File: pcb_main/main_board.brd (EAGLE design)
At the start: 160 x 100 mm, 14 parts, among them U1 STM32F411RET6

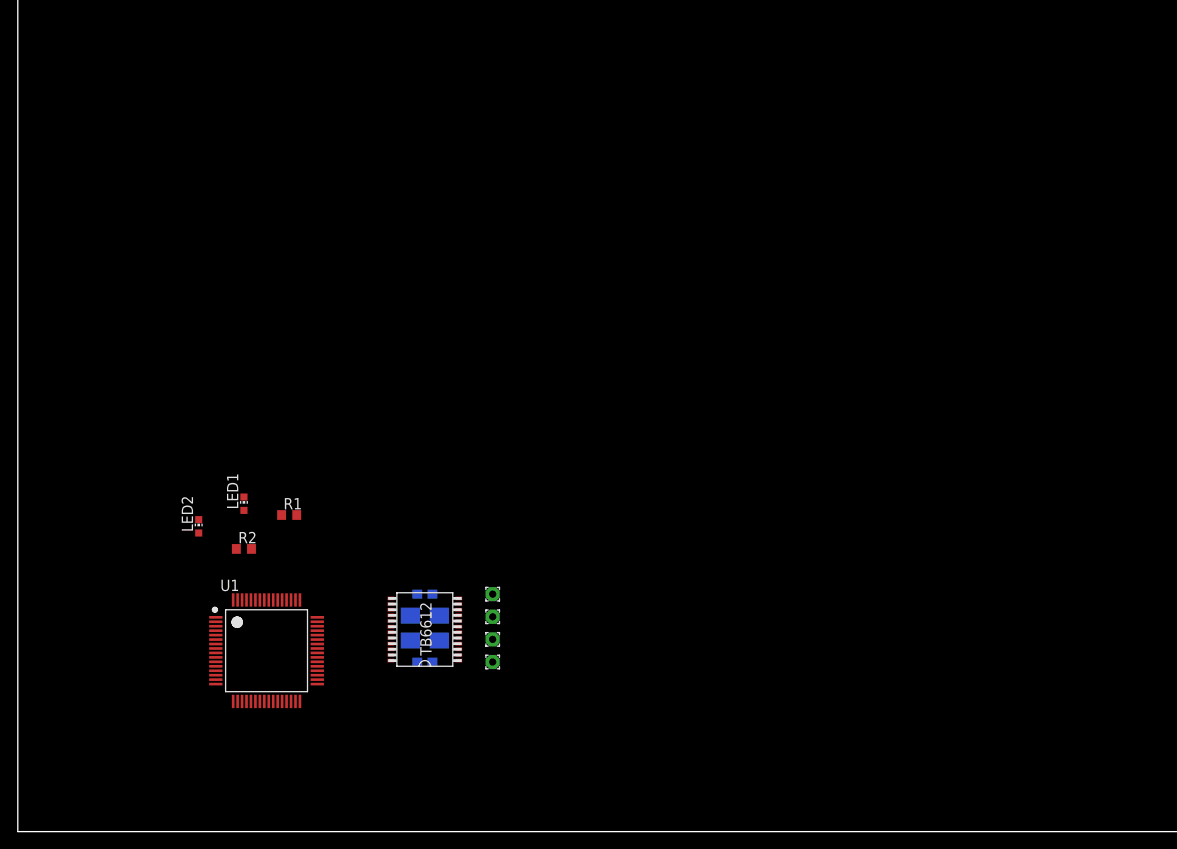
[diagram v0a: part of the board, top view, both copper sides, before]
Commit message: sensors on main pcb
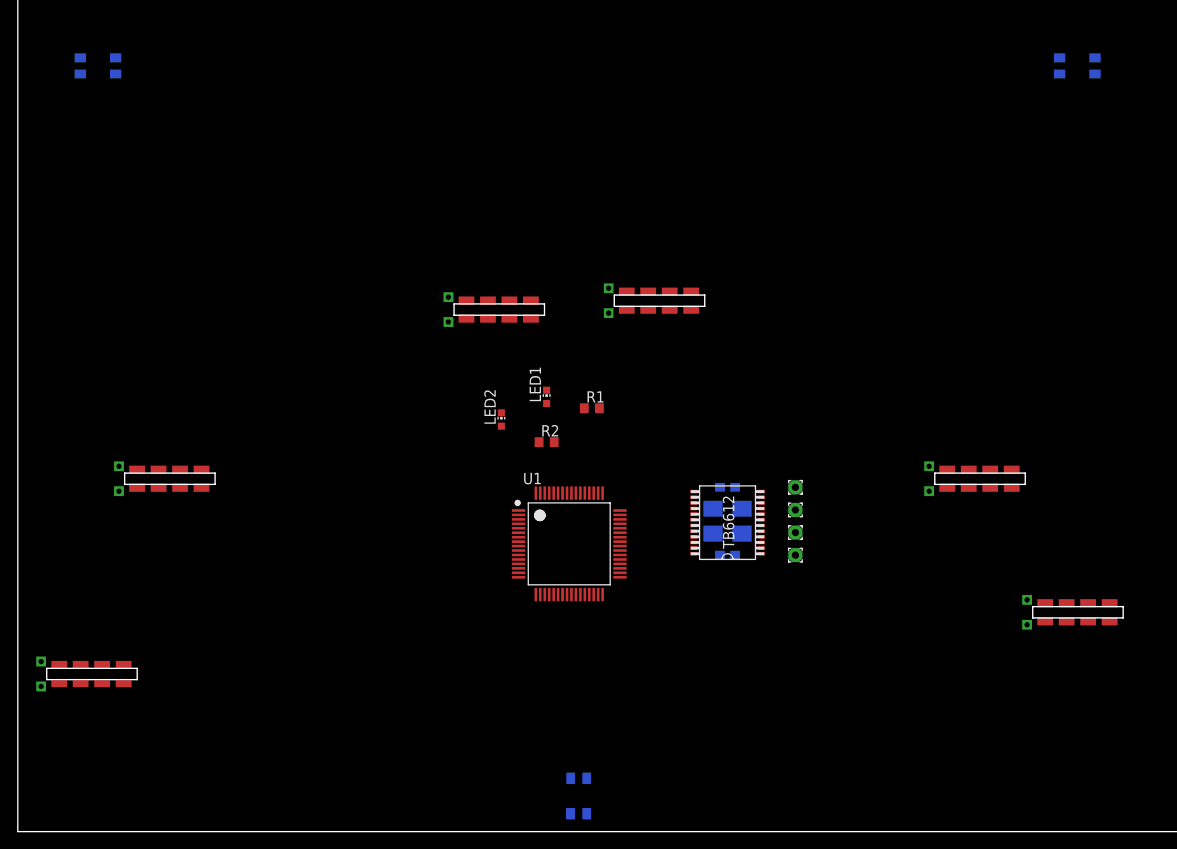
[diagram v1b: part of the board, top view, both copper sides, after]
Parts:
- added CZ1, CZ2, CZ3: KTIR0711S, KTIR0711S:TOP
- added U$1, U$2, U$3, U$4, U$5, U$6: TOF_VL53L0X, TOF_VL53L0X:TOF_VL53L0X
- moved C10 36.1 mm to (79.7, 33.5)
- moved C7 36.1 mm to (79.7, 38.7)
- moved C9 36.1 mm to (79.7, 31.1)
- moved H1 36.1 mm to (87.3, 31.1)
- moved H2 36.1 mm to (87.3, 33.6)
- moved H3 36.1 mm to (87.3, 38.7)
- moved H4 36.1 mm to (87.3, 36.1)
- moved LED1 36.1 mm to (59.4, 48.8)
- moved LED2 36.1 mm to (54.3, 46.3)
- moved R1 36.1 mm to (64.5, 47.6)
- moved R2 36.1 mm to (59.4, 43.8)
- moved TB6612 36.1 mm to (79.7, 34.9)
- moved U1 36.1 mm to (61.9, 32.3)
- moved C8 36.1 mm to (79.7, 36.3)
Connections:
- new net G1: U$1.G
- new net G2: U$2.G
- new net G3: U$3.G
- new net G4: U$6.G
- new net G5: U$5.G
- new net G6: U$4.G
- new net N$3: CZ1.ANODA, CZ2.KATODA
- new net N$4: CZ2.ANODA, CZ3.KATODA
- new net SCL: U$1.SCL, U$1.SCL_, U$2.SCL, U$2.SCL_, U$3.SCL, U$3.SCL_, U$4.SCL, U$4.SCL_, U$5.SCL, U$5.SCL_, U$6.SCL, U$6.SCL_
- new net SDA: U$1.SDA, U$1.SDA_, U$2.SDA, U$2.SDA_, U$3.SDA, U$3.SDA_, U$4.SDA, U$4.SDA_, U$5.SDA, U$5.SDA_, U$6.SDA, U$6.SDA_
- new net X1: U$1.X
- new net X2: U$2.X
- new net X3: U$3.X
- new net X4: U$6.X
- new net X5: U$5.X
- new net X6: U$4.X
- net 3,3V: now also U$1.VCC, U$1.VCC_, U$2.VCC, U$2.VCC_, U$3.VCC, U$3.VCC_, U$4.VCC, U$4.VCC_, U$5.VCC, U$5.VCC_, U$6.VCC, U$6.VCC_
- net GND: now also CZ1.EMITER, CZ2.EMITER, CZ3.EMITER, U$1.GND, U$1.GND_, U$2.GND, U$2.GND_, U$3.GND, U$3.GND_, U$4.GND, U$4.GND_, U$5.GND, U$5.GND_, U$6.GND, U$6.GND_

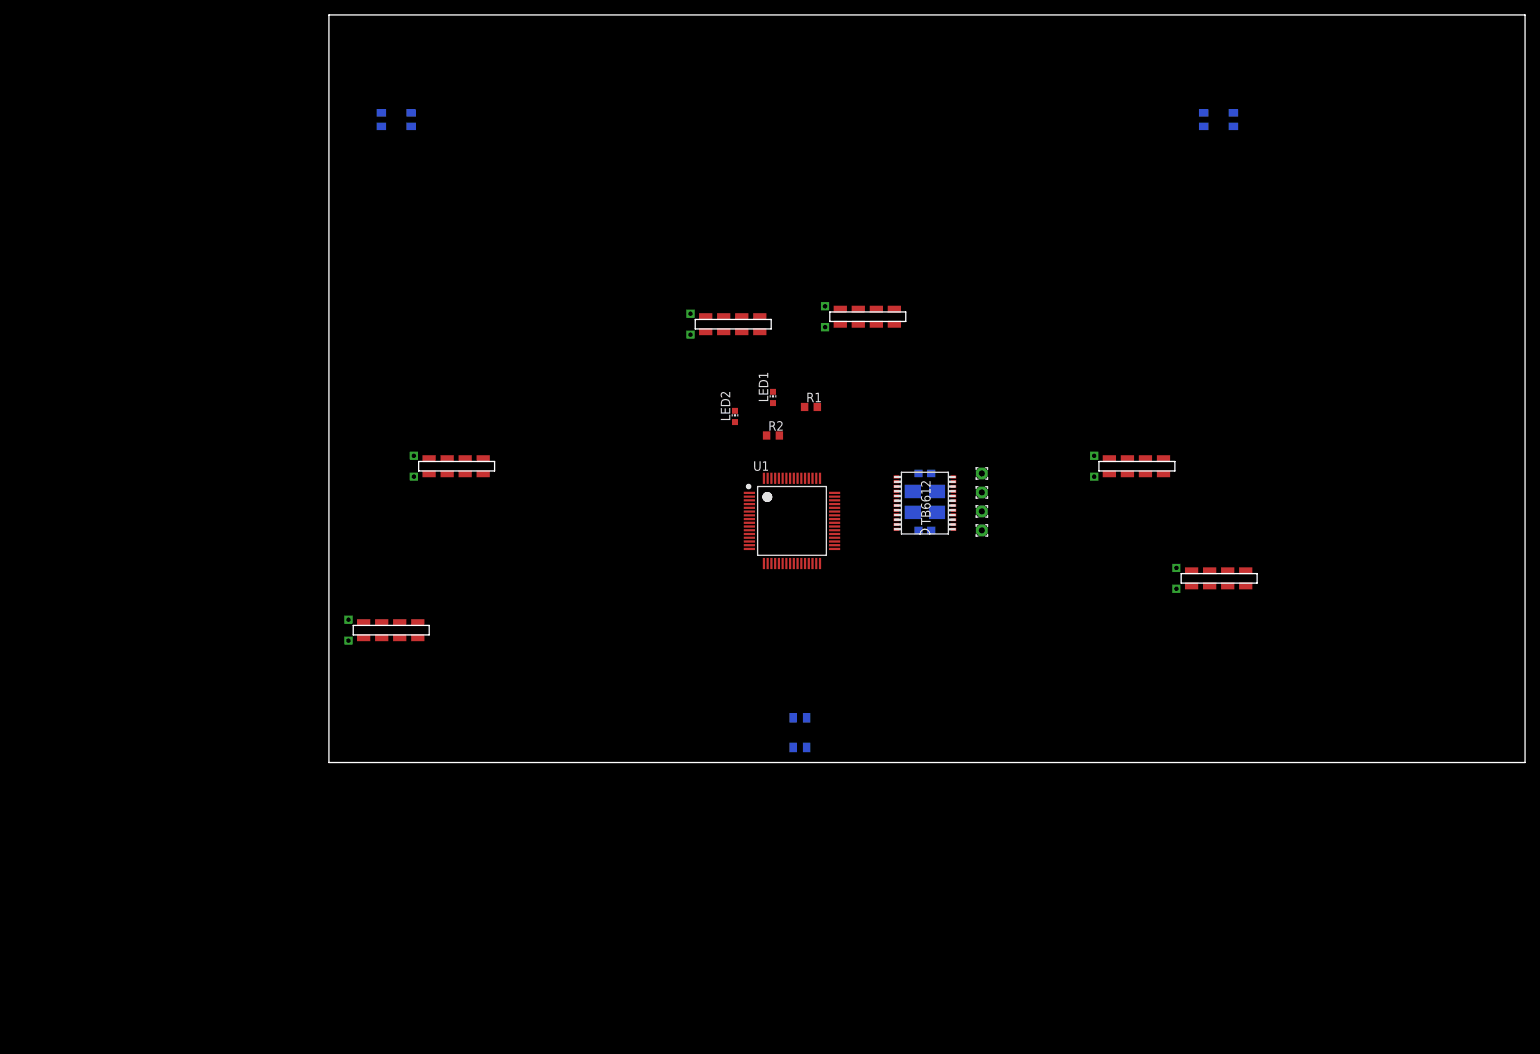
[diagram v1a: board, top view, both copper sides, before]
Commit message: pcb shape
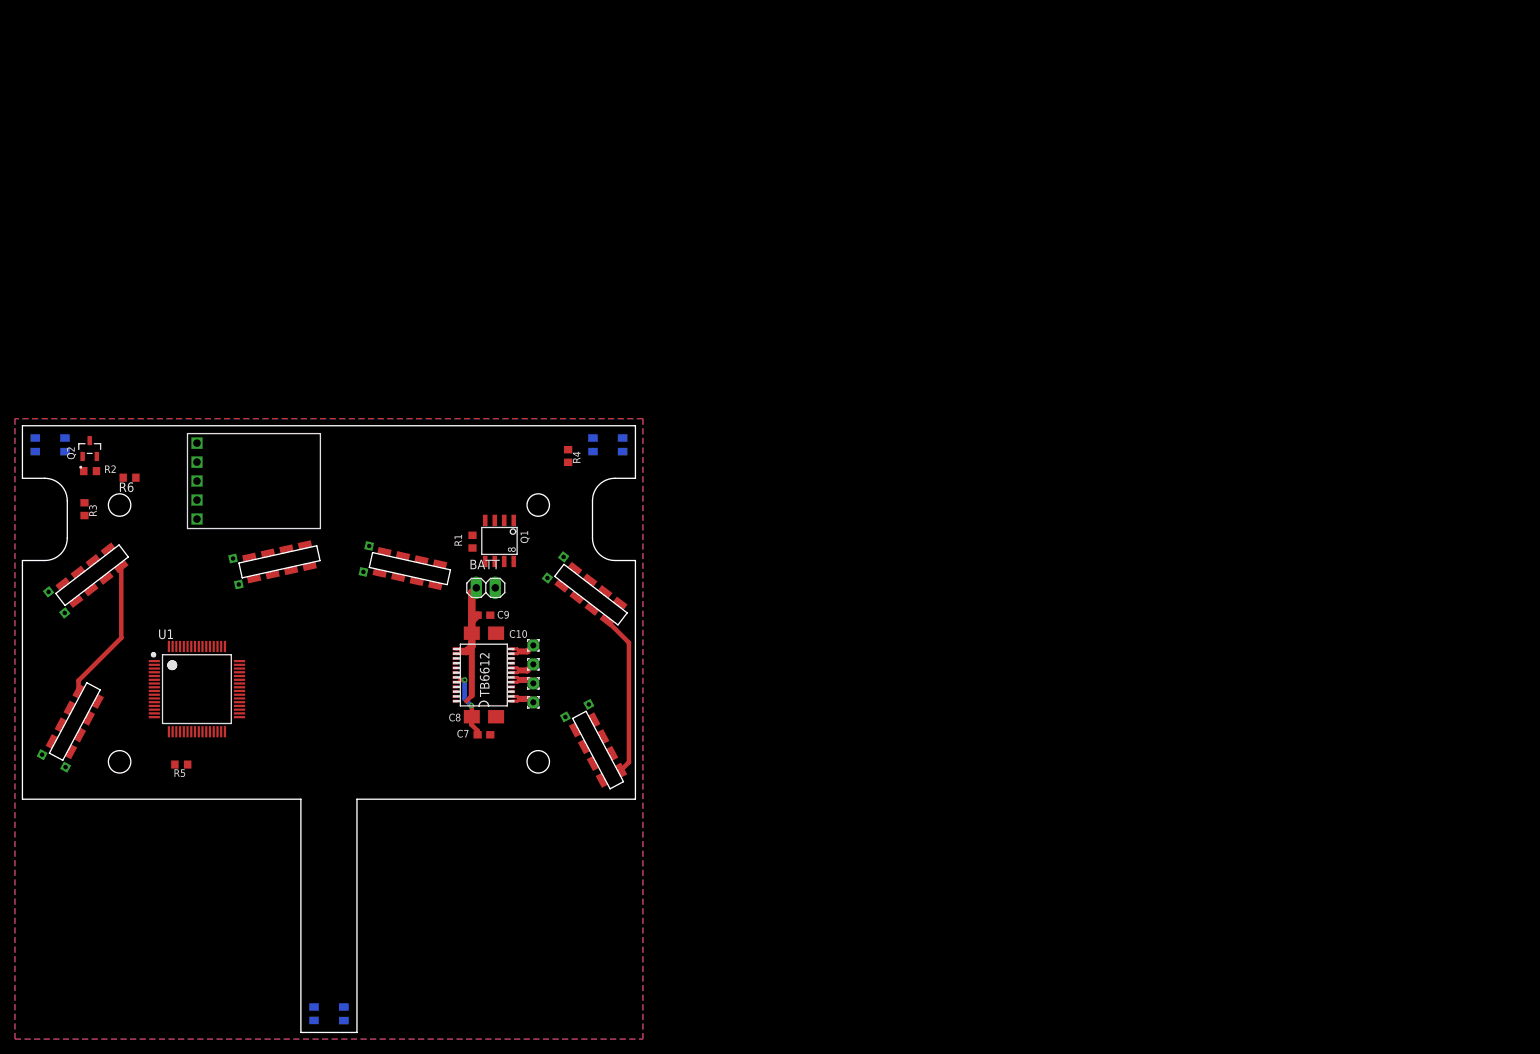
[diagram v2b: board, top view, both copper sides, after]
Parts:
- removed LED1, LED2: (no value), led:CHIP-LED0603
- added BATT: (no value), pinhead:1X02
- added Q1: FDS5680, transistor-fet:SO-8
- added Q2: 2N7002, 2N7002:SOT95P240X111-3N
- added R3, R4, R5: (no value), rcl:R0603
- added R6: 470R, rcl:R0603
- added U$7: D24V10F3-H, D24V10F3:D24V10F3-H
- R2: value (none) -> 10k
- moved CZ2 92.6 mm to (37.3, 42.5), turned to 180 degrees
- moved R2 91.5 mm to (-31.9, 39.0), turned to 180 degrees
- moved U$4 83.4 mm to (32.6, 5.90), turned to 298 degrees
- moved U1 82.7 mm to (-17.7, 9.82)
- moved U$5 74.2 mm to (30.2, 24.9), turned to 322.5 degrees
- moved CZ3 73.4 mm to (0.00, -33.6), turned to 180 degrees
- moved U$6 69.8 mm to (5.40, 26.1), turned to 347.5 degrees
- moved U$3 69.1 mm to (-11.6, 24.7), turned to 12.5 degrees
- moved C7 68.6 mm to (20.7, 3.71), flipped to the top, turned to 0 degrees
- moved C8 66.2 mm to (20.7, 6.12), flipped to the top, turned to 180 degrees
- moved H1 64.3 mm to (27.3, 8.05)
- moved H2 64.3 mm to (27.3, 10.6)
- moved H3 64.3 mm to (27.3, 15.7)
- moved H4 64.3 mm to (27.3, 13.1)
- moved CZ1 63.5 mm to (-37.3, 42.5), turned to 180 degrees
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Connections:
- net !A_DIR renamed A_DIR_1
- net A_DIR renamed A_DIR_2
- removed net +5V: C7.1, C8.+, TB6612.19, TB6612.20
- removed net +BAT: C10.+, C9.1, TB6612.13, TB6612.14, TB6612.24
- new net BAT+: BATT.2, C10.+, C9.1, R1.2, TB6612.13, TB6612.14, TB6612.24, U$7.VIN
- new net BAT-: BATT.1, Q1.5, Q1.6, Q1.7, Q1.8
- new net LS1: CZ1.KOLEKTOR, R3.1
- new net LS2: CZ2.KOLEKTOR, R4.1
- new net LS3: CZ3.KOLEKTOR, R5.1
- new net LS_ON/OFF: R6.1
- new net N$5: Q2.1, R2.2, R6.2
- net 3,3V: now also C7.1, C8.+, R3.2, R4.2, R5.2, TB6612.19, TB6612.20, U$7.VOUT
- net GND: now also Q1.1, Q1.2, Q1.3, Q2.2, R2.1, U$7.GND; no longer LED1.C, LED2.C
- net N$1: now also Q1.4; no longer LED1.A
- net N$2: now also CZ1.KATODA, Q2.3; no longer LED2.A, R2.1
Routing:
- net 3,3V: track 0.00 -> 50.6 mm, vias 0 -> 2
- net BAT+: track 0.00 -> 20.6 mm
- net BO2: track 0.00 -> 4.41 mm
- net BO1: track 0.00 -> 4.41 mm
- net AO2: track 0.00 -> 4.26 mm
- net AO: track 0.00 -> 4.26 mm
- added copper zone on layer 1, net GND
- added copper zone on layer 16, net GND
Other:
- board size 160 x 100 mm -> 82 x 81.2 mm

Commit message: power routed more or less
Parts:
- added OLED: (no value), pinhead:1X04
- added X1: FH12-14S-0.5SH, con-hirose:FH12-14S-0.5SH
- moved U$7 33.8 mm to (6.28, 21.5), turned to 180 degrees
- moved R5 10.2 mm to (-9.59, 1.00)
- moved R1 9.83 mm to (22.1, 20.2), flipped to the bottom, turned to 180 degrees
- moved BATT 4.39 mm to (18.5, 19.7), turned to 270 degrees
- moved Q1 4.32 mm to (23.0, 25.3), turned to 180 degrees
- moved C8 4.02 mm to (24.5, 7.39)
- moved TB6612 4.02 mm to (24.5, 13.1)
- moved C10 4.02 mm to (24.5, 18.6)
- moved C7 4.02 mm to (24.5, 4.98)
- moved H1 4.02 mm to (31.1, 9.32)
- moved H2 4.02 mm to (31.1, 11.9)
- moved H3 4.02 mm to (31.1, 16.9)
- moved H4 4.02 mm to (31.1, 14.4)
- moved C9 4.00 mm to (24.5, 20.9)
- moved U1 3.59 mm to (-15.1, 12.4)
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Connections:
- net !B_DIR renamed B_DIR_1
- net B_DIR renamed B_DIR_2
- net LS_ON/OFF renamed LS_ON
- removed net N$1: Q1.4, R1.1
- new net LED: X1.7
- new net ROBOT_OFF: Q1.4, R1.1, X1.2
- new net RST: X1.8
- new net SW1: X1.3
- new net SW2: X1.4
- new net SW3: X1.5
- new net SW4: X1.6
- new net SWCLK: X1.10
- new net SWDIO: X1.9
- new net VCC: OLED.4
- net 3,3V: now also X1.14
- net GND: now also OLED.3, X1.1
- net SCL: now also OLED.2
- net SDA: now also OLED.1
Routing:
- net 3,3V: track 50.6 -> 133.4 mm
- net BAT+: track 20.6 -> 45.2 mm, vias 0 -> 1
- net SDA: track 0.00 -> 21.4 mm
- net SCL: track 0.00 -> 20.9 mm
- net BAT-: track 0.00 -> 15.3 mm
- net ROBOT_OFF: track 0.00 -> 10.3 mm, vias 0 -> 1

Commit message: almost there
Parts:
- removed Q2: 2N7002, 2N7002:SOT95P240X111-3N
- added C1, C2: 22p, rcl:C0603
- added C11, C12, C13, C15, C3, C6: 100n, rcl:C0603
- added C14, C5: 4u7, rcl:C0603
- added C4: 1u, rcl:C0603
- added JP1: (no value), pinhead:1X03
- added R10, R11, R12, R13, R9: 4k7, rcl:R0603
- added R14: 100R, rcl:R0603
- added R7, R8: (no value), rcl:R0603
- added S2: DTSM-3, switch-tact:DTSM-3
- added T1: BC847, transistor:SOT23
- added U$8: 8MHz, CRYSTAL_SMD_3,4x2.7mm:CRYSTAL_3,4X2,7
- OLED: value (none) -> B4B-XH; device pinhead:1X04 -> jst connectors:JST_B4B-XH-A(LF)(SN)
- R1: value (none) -> 10k
- R2: value 10k -> 130R
- R6: value 470R -> 4k7
- moved R6 37.0 mm to (-14.0, 3.81), flipped to the bottom, turned to 90 degrees
- moved R3 31.2 mm to (-1.46, 33.5), flipped to the bottom
- moved U$7 21.4 mm to (5.34, 42.9), turned to 270 degrees
- moved R5 15.8 mm to (6.11, -1.08), turned to 270 degrees
- moved U1 15.2 mm to (0.12, 12.4), turned to 45 degrees
- moved R2 14.2 mm to (-16.5, 40.3), turned to 0 degrees
- moved R4 14.1 mm to (19.8, 33.9), flipped to the bottom
- moved X1 3.81 mm to (14.0, 3.81)
- moved OLED 1.27 mm to (-17.8, 0.00), turned to 180 degrees
- moved CZ1 0.34 mm to (-37.6, 42.6), turned to 0 degrees
- moved CZ2 0.34 mm to (37.6, 42.6), turned to 0 degrees
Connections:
- removed net 3,3V_ADC: U1.13
- removed net SCL: OLED.2, U$1.SCL, U$1.SCL_, U$2.SCL, U$2.SCL_, U$3.SCL, U$3.SCL_, U$4.SCL, U$4.SCL_, U$5.SCL, U$5.SCL_, U$6.SCL, U$6.SCL_
- removed net SDA: OLED.1, U$1.SDA, U$1.SDA_, U$2.SDA, U$2.SDA_, U$3.SDA, U$3.SDA_, U$4.SDA, U$4.SDA_, U$5.SDA, U$5.SDA_, U$6.SDA, U$6.SDA_
- new net BAT_MEAS: R7.2, R8.1, U1.27
- new net N$6: R2.1, T1.2
- new net N$7: U1.57
- new net RX: U1.17
- new net SCL_1: R10.1, U$1.SCL, U$1.SCL_, U$2.SCL, U$2.SCL_, U$3.SCL, U$3.SCL_, U1.58
- new net SCL_2: OLED.2, R11.1, U1.29
- new net SCL_3: R13.1, U$4.SCL, U$4.SCL_, U$5.SCL, U$5.SCL_, U$6.SCL, U$6.SCL_, U1.41
- new net SDA_1: R9.1, U$1.SDA, U$1.SDA_, U$2.SDA, U$2.SDA_, U$3.SDA, U$3.SDA_, U1.59
- new net SDA_2: OLED.1, R6.1, U1.55
- new net SDA_3: R12.1, U$4.SDA, U$4.SDA_, U$5.SDA, U$5.SDA_, U$6.SDA, U$6.SDA_, U1.40
- new net SERVO: JP1.3, U1.15
- new net TX: U1.16
- new net VCAP: C5.1, U1.30
- new net XTAL1: C2.1, U$8.CRST1, U1.5
- new net XTAL2: C1.1, U$8.CRST2, U1.6
- net 3,3V: now also C11.1, C12.1, C13.1, C14.1, C3.1, C4.1, C6.1, OLED.4, R10.2, R11.2, R12.2, R13.2, R6.2, R9.2, U1.13, X1.1; no longer X1.14
- net A_DIR_1: now also U1.25
- net A_DIR_2: now also U1.24
- net BAT+: now also CZ3.ANODA, R7.1
- net B_DIR_1: now also U1.26
- net B_DIR_2: now also U1.28
- net GND: now also C1.2, C11.2, C12.2, C13.2, C14.2, C15.2, C2.2, C3.2, C4.2, C5.2, C6.2, JP1.1, R2.2, R8.2, S2.2, U$8.GND, U$8.GND2, U1.60, X1.14; no longer Q2.2, R2.1, X1.1
- net LED: now also X1.8; no longer X1.7
- net LS1: now also U1.9
- net LS2: now also U1.10
- net LS3: now also U1.11
- net LS_ON: now also R14.1, U1.52; no longer R6.1
- net N$2: now also T1.3; no longer Q2.3
- net N$5: now also R14.2, T1.1; no longer Q2.1, R2.2, R6.2
- net PWMA: now also U1.22
- net PWMB: now also U1.23
- net ROBOT_OFF: now also X1.13; no longer X1.2
- net RST: now also C15.1, S2.1, U1.7, X1.7; no longer X1.8
- net SW1: now also X1.12; no longer X1.3
- net SW2: now also X1.11; no longer X1.4
- net SW3: now also X1.10; no longer X1.5
- net SW4: now also X1.9; no longer X1.6
- net SWCLK: now also U1.49, X1.5; no longer X1.10
- net SWDIO: now also U1.46, X1.6; no longer X1.9
- net VCC: now also JP1.2; no longer OLED.4
- net X1: now also U1.4
- net X2: now also U1.3
- net X3: now also U1.2
- net X4: now also U1.45
- net X5: now also U1.35
- net X6: now also U1.34
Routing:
- net 3,3V: track 133.4 -> 263.5 mm, vias 2 -> 12
- net N$4: track 0.00 -> 116.1 mm
- net LS2: track 0.00 -> 73.5 mm, vias 0 -> 4
- net N$3: track 0.00 -> 72.3 mm
- net LS1: track 0.00 -> 71.5 mm, vias 0 -> 3
- net SCL_1: track 0.00 -> 65.3 mm, vias 0 -> 2
- net SDA_1: track 0.00 -> 64.9 mm, vias 0 -> 3
- net SDA_3: track 0.00 -> 63.6 mm, vias 0 -> 6
- net SCL_3: track 0.00 -> 62.9 mm, vias 0 -> 4
- net RST: track 0.00 -> 46.2 mm, vias 0 -> 4
- net X5: track 0.00 -> 34.6 mm
- net X2: track 0.00 -> 34.3 mm, vias 0 -> 1
- net X1: track 0.00 -> 34.1 mm, vias 0 -> 1
- net SCL_2: track 0.00 -> 32.7 mm, vias 0 -> 2
- net X6: track 0.00 -> 32.5 mm, vias 0 -> 1
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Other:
- board text added: "3,3V"
- board text added: "GND"
- board text added: "SCL"
- board text added: "SDA"

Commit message: before 2 H-bridges
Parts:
- added R15: 130R, rcl:R0603
- moved R5 13.6 mm to (-7.43, -0.27), turned to 180 degrees
- moved C15 0.76 mm to (-18.3, 15.1)
- moved S2 0.76 mm to (-18.3, 15.1)
- flipped JP1 to the top, turned to 180 degrees
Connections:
- net 3,3V: now also R15.1
- net RST: now also R15.2
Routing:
- net BAT+: track 59.1 -> 120.7 mm, vias 1 -> 2
- net 3,3V: track 263.5 -> 324.8 mm, vias 12 -> 17
- net LS3: track 0.00 -> 48.5 mm, vias 0 -> 2
- net TX: track 0.00 -> 9.18 mm, vias 0 -> 1
- net RX: track 0.00 -> 7.72 mm, vias 0 -> 1
- net RST: track 46.2 -> 49.5 mm
- net SCL_2: track 32.7 -> 33.7 mm
- net BAT-: track 14.7 -> 14.0 mm
- net X3: track 18.4 -> 17.8 mm
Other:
- board text added: "Miras V1.0 minisumo Dominik Pluta Kamil Winnicki"
